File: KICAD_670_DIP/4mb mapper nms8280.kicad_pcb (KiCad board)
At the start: 2 copper layers, 102.2 x 68.2 mm, 28 parts, among them IC131 74LS125, IC131B1 74LS125, IC131C1 74LS125, IC147 74LS157, IC147B1 74LS157, IC149 74LS670, IC149B1 74LS670, IC157B1 74LS08, IC180B1 74LS00, J1 Conn_01x10_Pin, U1 HY5117404B, U2 HY5117404B

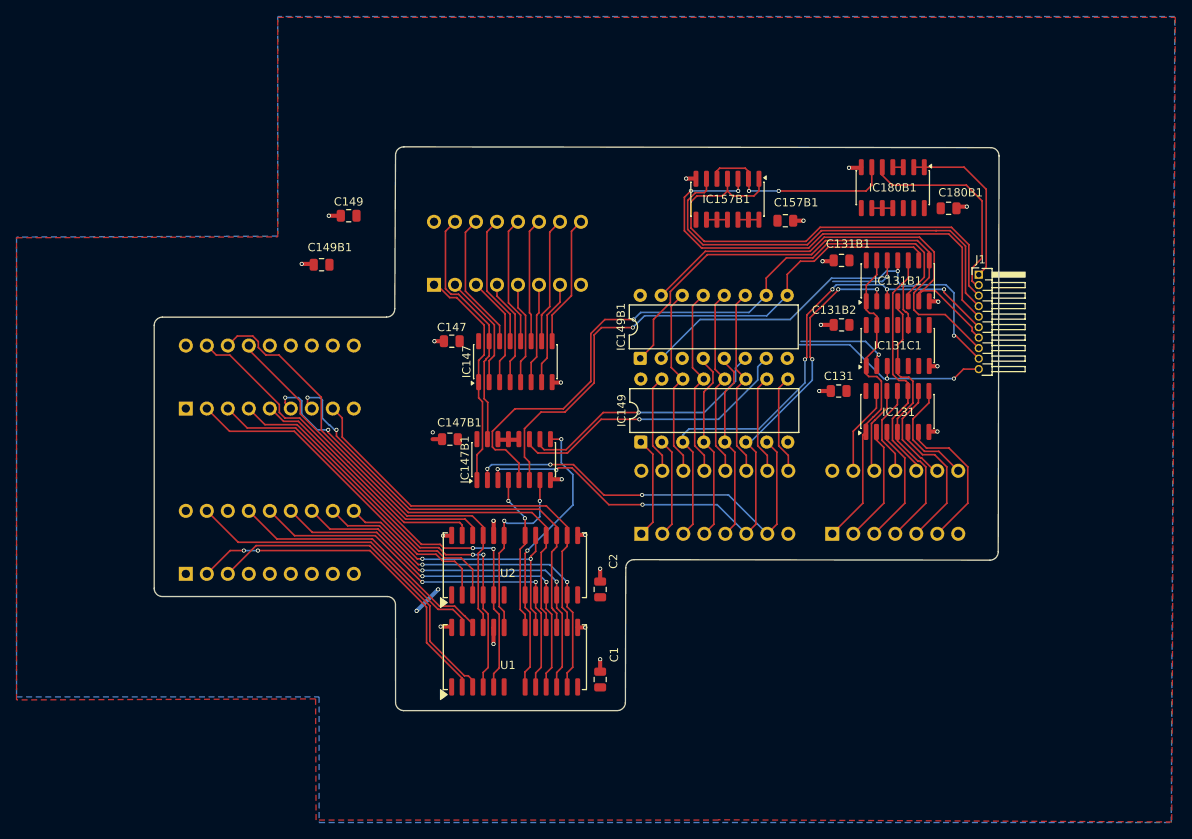
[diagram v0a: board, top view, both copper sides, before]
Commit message: Update 670 DIP PCB silkscreen and photos
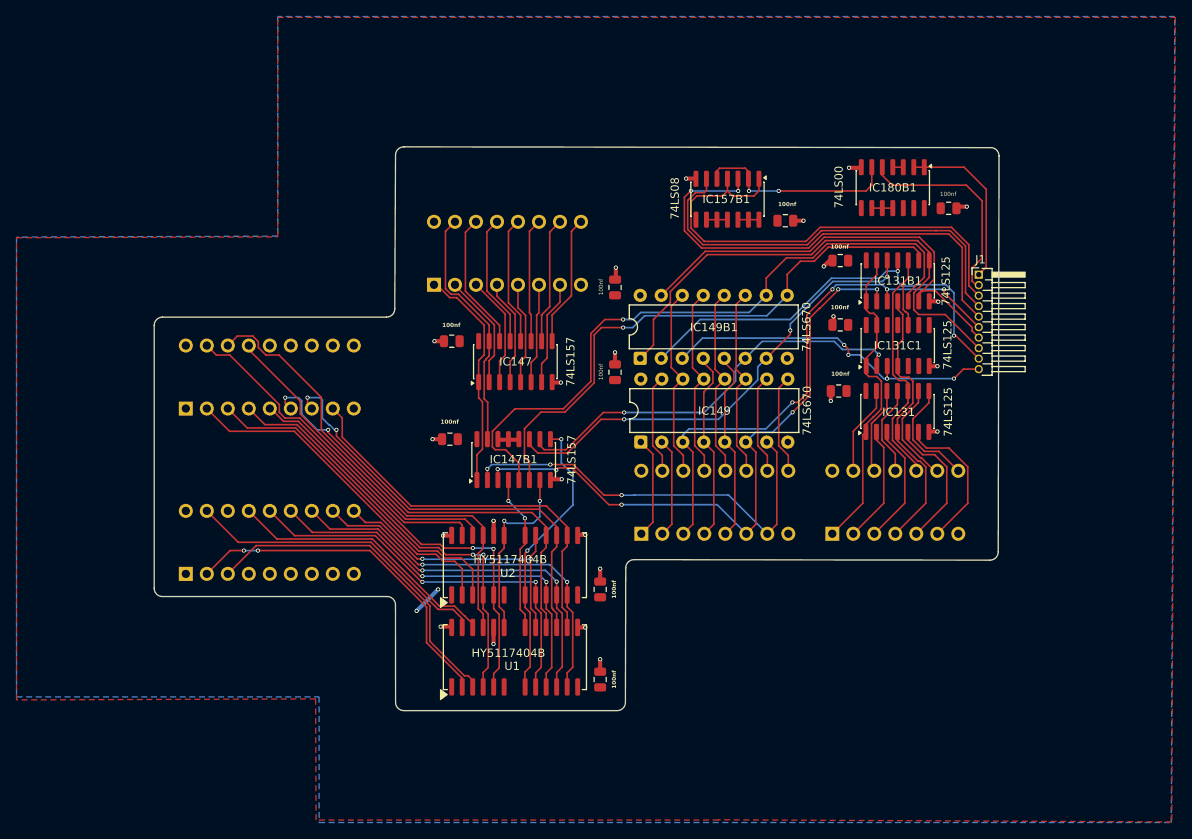
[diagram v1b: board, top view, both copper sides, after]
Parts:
- moved C149 37.4 mm to (153.8, 90.2), turned to 90 degrees
- moved C149B1 35.6 mm to (153.8, 80.0), turned to 90 degrees
- moved C131B1 0.15 mm to (181.1, 76.7)
- moved C131B2 0.15 mm to (181.1, 84.5)
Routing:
- net Net-(IC131C1-1O): track 25.4 -> 41.3 mm, vias 2 -> 4
- net Net-(IC131B1-4D): track 45.0 -> 57.6 mm, vias 2 -> 3
- net Net-(IC131C1-1D): track 43.6 -> 51.2 mm
- net /4mb mapper nms8280/IC149_P6: track 76.8 -> 78.0 mm
- net /4mb mapper nms8280/IC149_P3: track 64.8 -> 65.7 mm
- net GND: track 31.7 -> 31.1 mm
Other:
- board text added: "J1 - to IC180 pin 12 J2 - to R130 J3 - to IC111 pin 2 J4 - to R127 J5 - to R128 J6 - to IC161 pin 11 J7 - to IC176 pin 11 J8 - to IC176 pin 13 J9 - to IC178 pin 5 J10 - to IC178 pin 7"
